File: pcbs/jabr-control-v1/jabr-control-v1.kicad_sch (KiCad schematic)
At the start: 0 parts

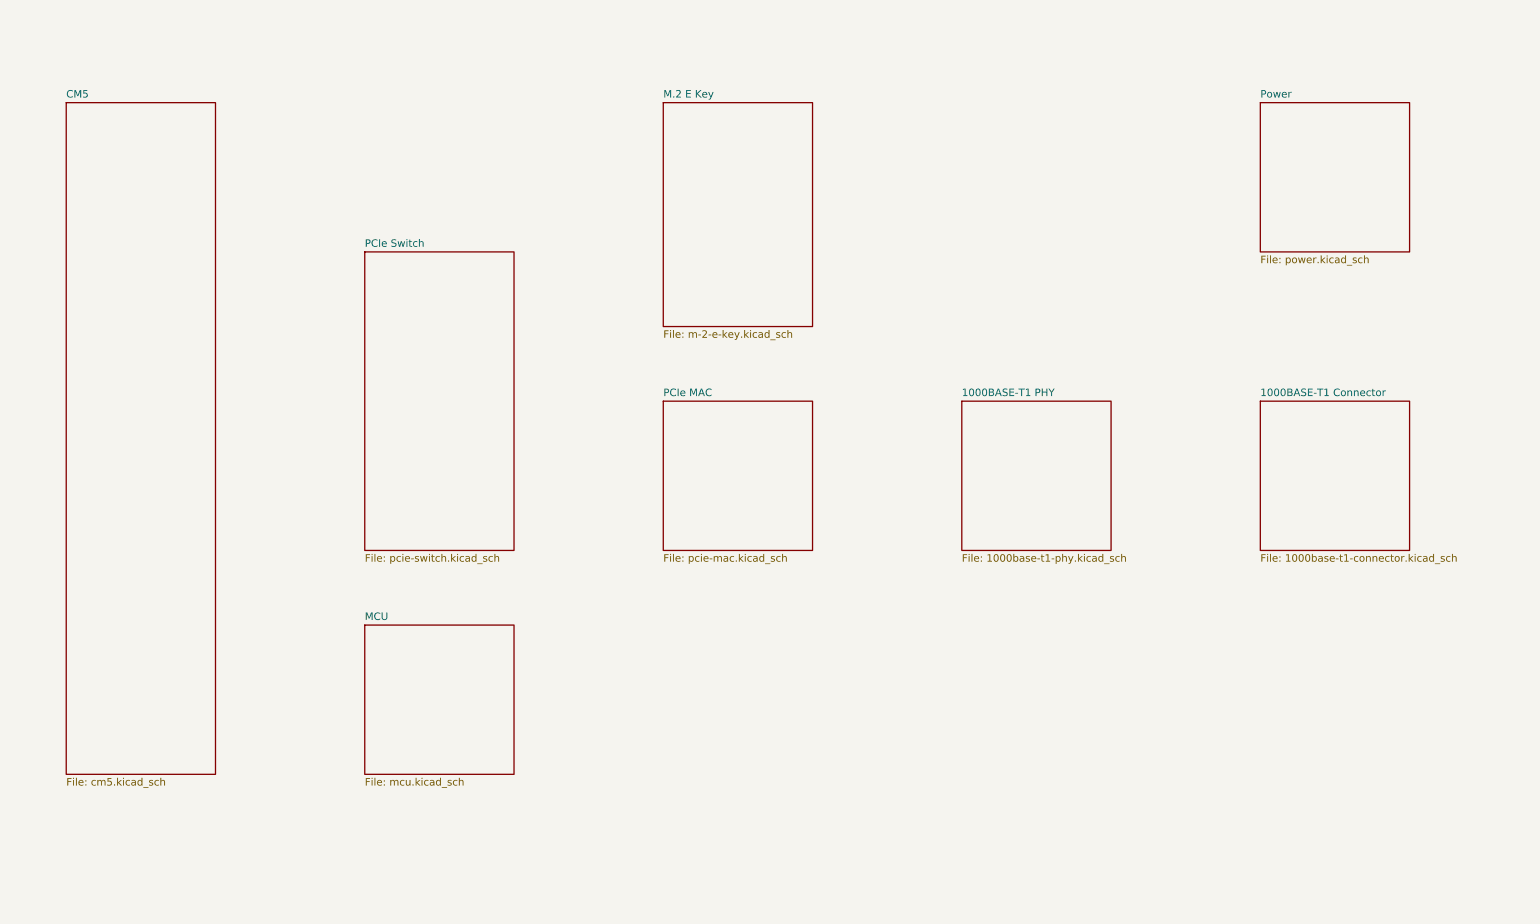
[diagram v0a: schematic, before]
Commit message: Added PCIe connections
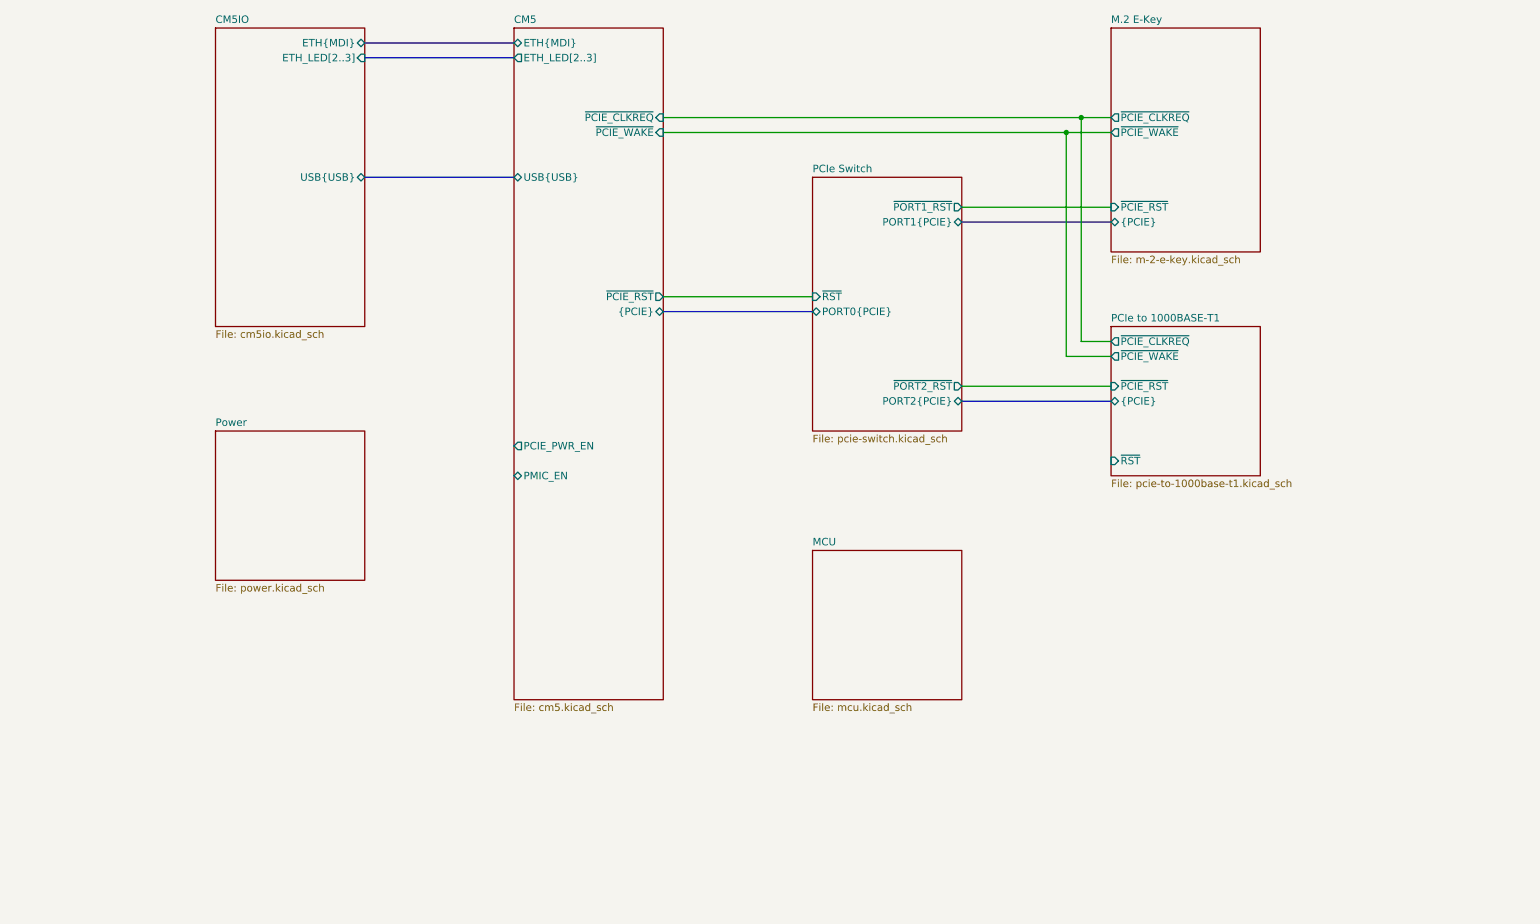
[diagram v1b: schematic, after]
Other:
- sheet M.2 E Key renamed M.2 E-Key
- removed sheet 1000BASE-T1 Connector
- removed sheet 1000BASE-T1 PHY
- removed sheet PCIe MAC
- added sheet CM5IO (cm5io.kicad_sch)
- added sheet PCIe to 1000BASE-T1 (pcie-to-1000base-t1.kicad_sch)
- sheet CM5 ports: added ETH_LED[2..3], ETH{MDI}, PCIE_PWR_EN, PMIC_EN, USB{USB}, {PCIE}, ~{PCIE_CLKREQ}, ~{PCIE_RST}, ~{PCIE_WAKE}; removed none
- sheet M.2 E-Key ports: added {PCIE}, ~{PCIE_CLKREQ}, ~{PCIE_RST}, ~{PCIE_WAKE}; removed none
- sheet PCIe Switch ports: added PORT0{PCIE}, PORT1{PCIE}, PORT2{PCIE}, ~{PORT1_RST}, ~{PORT2_RST}, ~{RST}; removed none

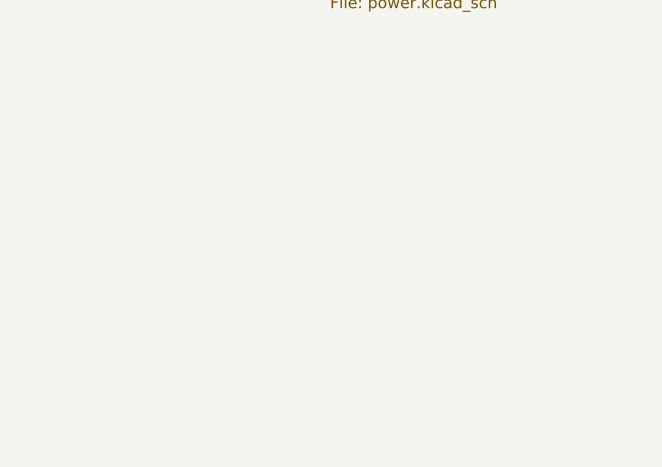
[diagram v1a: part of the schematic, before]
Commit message: Added power sheets
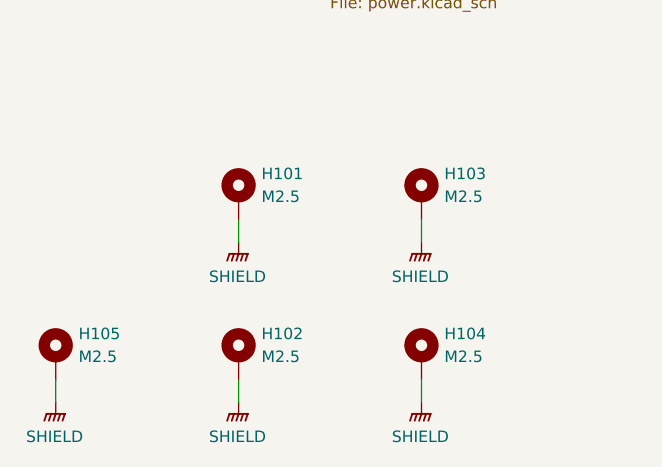
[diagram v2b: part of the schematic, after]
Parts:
- added H101, H102, H103, H104, H105: M2.5, MountingHole:MountingHole_2.7mm_M2.5_Pad, symbol Mechanical:MountingHole_Pad
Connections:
- new net SHIELD: H101.1, H102.1, H103.1, H104.1, H105.1

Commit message: Worked on power and other areas of the schematic
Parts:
- removed H104: M2.5, MountingHole:MountingHole_2.7mm_M2.5_Pad, symbol Mechanical:MountingHole_Pad
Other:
- removed sheet MCU
- sheet CM5 ports: added VBUS_EN, ~{RST}; removed PMIC_EN
- sheet PCIe to 1000BASE-T1 ports: added INH; removed none
- sheet Power ports: added 3V3_M2_EN, INH; removed none
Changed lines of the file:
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@@
 	(wire
 		(pts
-			(xy 73.66 175.26) (xy 73.66 177.8)
+			(xy 139.7 116.84) (xy 215.9 116.84)
 		)
 		(stroke
@@
 	(wire
 		(pts
+			(xy 88.9 109.22) (xy 114.3 109.22)
+		)
+		(stroke
+			(width 0)
+			(type default)
+		)
+	)
+	(wire
+		(pts
 			(xy 210.82 91.44) (xy 210.82 53.34)
 		)
@@
 		(pts
 			(xy 190.5 99.06) (xy 215.9 99.06)
+		)
+		(stroke
+			(width 0)
+			(type default)
+		)
+	)
+	(wire
+		(pts
+			(xy 88.9 129.54) (xy 215.9 129.54)
 		)
 		(stroke
@@
 	)
 	(symbol
-		(lib_id "PWR-SYM:SHIELD")
-		(at 73.66 177.8 0)
-		(unit 1)
-		(exclude_from_sim no)
-		(in_bom yes)
-		(on_board yes)
-		(dnp no)
-		(fields_autoplaced yes)
-		(property "Reference" "#PWR0108"
-			(at 73.66 182.88 0)
-			(effects
-				(font
-					(size 1.27 1.27)
-				)
-				(hide yes)
-			)
-		)
-		(property "Value" "SHIELD"
-			(at 73.533 181.61 0)
-			(effects
-				(font
-					(size 1.27 1.27)
-				)
-			)
-		)
-		(property "Footprint" ""
-			(at 73.66 179.07 0)
-			(effects
-				(font
-					(size 1.27 1.27)
-				)
-				(hide yes)
-			)
-		)
-		(property "Datasheet" ""
-			(at 73.66 179.07 0)
-			(effects
-				(font
-					(size 1.27 1.27)
-				)
-				(hide yes)
-			)
-		)
-		(property "Description" "Power symbol creates a global label with name \"SHIELD\" , global ground"
-			(at 73.66 177.8 0)
-			(effects
-				(font
-					(size 1.27 1.27)
-				)
-				(hide yes)
-			)
-		)
-		(pin "1"
-		)
-		(instances
-			(project "jabr-control-v1"
-				(path "/f91ec272-d09a-4038-bbbb-962739a92c51"
-					(reference "#PWR0108")
-					(unit 1)
-				)
-			)
-		)
-	)
-	(symbol
 		(lib_id "Mechanical:MountingHole_Pad")
 		(at 53.34 172.72 0)
@@
 	(symbol
 		(lib_id "Mechanical:MountingHole_Pad")
-		(at 73.66 172.72 0)
-		(unit 1)
-		(exclude_from_sim no)
-		(in_bom no)
-		(on_board yes)
-		(dnp no)
-		(fields_autoplaced yes)
-		(property "Reference" "H104"
-			(at 76.2 170.1799 0)
-			(effects
-				(font
-					(size 1.27 1.27)
-				)
-				(justify left)
-			)
-		)
-		(property "Value" "M2.5"
-			(at 76.2 172.7199 0)
-			(effects
-				(font
-					(size 1.27 1.27)
-				)
-				(justify left)
-			)
-		)
-		(property "Footprint" "MountingHole:MountingHole_2.7mm_M2.5_Pad"
-			(at 73.66 172.72 0)
-			(effects
-				(font
-					(size 1.27 1.27)
-				)
-				(hide yes)
-			)
-		)
-		(property "Datasheet" "~"
-			(at 73.66 172.72 0)
-			(effects
-				(font
-					(size 1.27 1.27)
-				)
-				(hide yes)
-			)
-		)
-		(property "Description" "Mounting Hole with connection"
-			(at 73.66 172.72 0)
-			(effects
-				(font
-					(size 1.27 1.27)
-				)
-				(hide yes)
-			)
-		)
-		(pin "1"
-		)
-		(instances
-			(project "jabr-control-v1"
-				(path "/f91ec272-d09a-4038-bbbb-962739a92c51"
-					(reference "H104")
-					(unit 1)
-				)
-			)
-		)
-	)
-	(symbol
-		(lib_id "Mechanical:MountingHole_Pad")
 		(at 33.02 172.72 0)
 		(unit 1)
@@
 	)
 	(sheet
-		(at 165.1 127)
-		(size 25.4 25.4)
-		(exclude_from_sim no)
-		(in_bom yes)
-		(on_board yes)
-		(dnp no)
-		(fields_autoplaced yes)
-		(stroke
-			(width 0.1524)
-			(type solid)
-		)
-		(fill
-			(color 0 0 0 0.0000)
-		)
-		(property "Sheetname" "MCU"
-			(at 165.1 126.2884 0)
-			(effects
-				(font
-					(size 1.27 1.27)
-				)
-				(justify left bottom)
-			)
-		)
-		(property "Sheetfile" "mcu.kicad_sch"
-			(at 165.1 152.9846 0)
-			(effects
-				(font
-					(size 1.27 1.27)
-				)
-				(justify left top)
-			)
-		)
-		(instances
-			(project "jabr-control-v1"
-				(path "/f91ec272-d09a-4038-bbbb-962739a92c51"
-					(page "7")
-				)
-			)
-		)
-	)
-	(sheet
 		(at 215.9 38.1)
 		(size 25.4 38.1)
@@
 	(sheet
 		(at 215.9 88.9)
-		(size 25.4 25.4)
+		(size 25.4 43.18)
 		(exclude_from_sim no)
 		(in_bom yes)
@@
 		)
 		(property "Sheetfile" "pcie-to-1000base-t1.kicad_sch"
-			(at 215.9 114.8846 0)
+			(at 215.9 132.6646 0)
 			(effects
 				(font
@@
 		)
 		(pin "~{RST}" input
-			(at 215.9 111.76 180)
+			(at 215.9 116.84 180)
+			(effects
+				(font
+					(size 1.27 1.27)
+				)
+				(justify left)
+			)
+		)
+		(pin "INH" output
+			(at 215.9 129.54 180)
 			(effects
 				(font
@@
 			)
 		)
+		(pin "3V3_M2_EN" input
+			(at 88.9 109.22 0)
+			(effects
+				(font
+					(size 1.27 1.27)
+				)
+				(justify right)
+			)
+		)
+		(pin "INH" input
+			(at 88.9 129.54 0)
+			(effects
+				(font
+					(size 1.27 1.27)
+				)
+				(justify right)
+			)
+		)
 		(instances
 			(project "jabr-control-v1"
@@
 	(sheet
 		(at 114.3 38.1)
-		(size 25.4 114.3)
+		(size 25.4 81.28)
 		(exclude_from_sim no)
 		(in_bom yes)
@@
 		)
 		(property "Sheetfile" "cm5.kicad_sch"
-			(at 114.3 152.9846 0)
+			(at 114.3 119.9646 0)
 			(effects
 				(font
@@
 			)
 		)
-		(pin "PMIC_EN" bidirectional
-			(at 114.3 114.3 180)
-			(effects
-				(font
-					(size 1.27 1.27)
-				)
-				(justify left)
-			)
-		)
+		(pin "VBUS_EN" output
+			(at 114.3 66.04 180)
+			(effects
+				(font
+					(size 1.27 1.27)
+				)
+				(justify left)
+			)
+		)
+		(pin "~{RST}" output
+			(at 139.7 116.84 0)
+			(effects
+				(font
+					(size 1.27 1.27)
+				)
+				(justify right)
+			)
+		)

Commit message: Various small updates
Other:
- sheet CM5 ports: added I2C2{I2C}; removed none
- sheet PCIe Switch ports: added SMB{I2C}; removed none
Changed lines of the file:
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@@
+		)
+	)
+	(bus
+		(pts
+			(xy 139.7 91.44) (xy 165.1 91.44)
+		)
+		(stroke
+			(width 0)
+			(type default)
 		)
 	)
@@
 			)
 		)
+		(pin "SMB{I2C}" bidirectional
+			(at 165.1 91.44 180)
+			(effects
+				(font
+					(size 1.27 1.27)
+				)
+				(justify left)
+			)
+		)
 		(instances
 			(project "jabr-control-v1"
@@
 			(effects
 				(font
+					(size 1.27 1.27)
+				)
+				(justify right)
+			)
+		)
+		(pin "I2C2{I2C}" bidirectional
+			(at 139.7 91.44 0)
+			(effects
+				(font

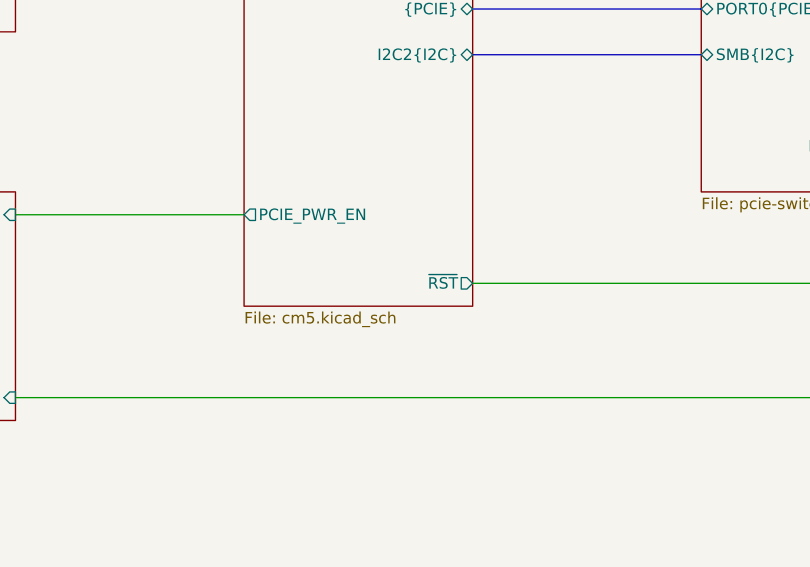
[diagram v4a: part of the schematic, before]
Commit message: Progress on LAN7431 power
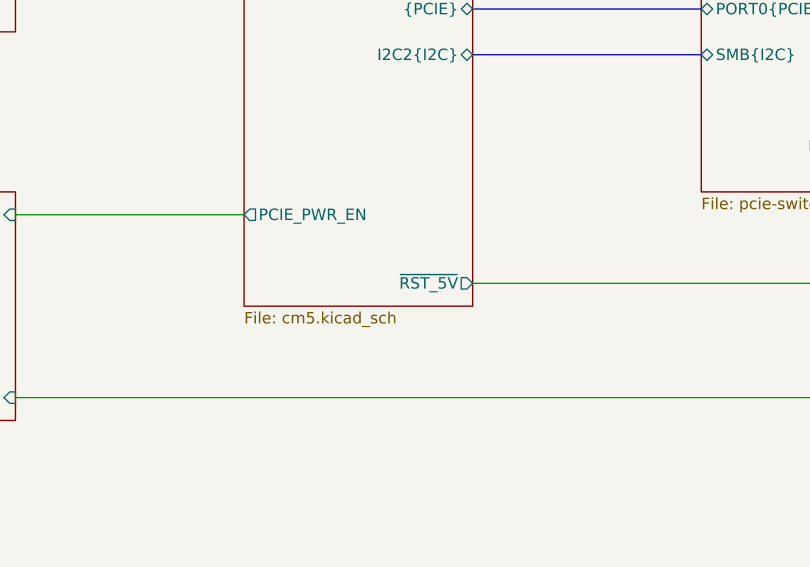
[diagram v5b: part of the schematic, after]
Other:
- sheet CM5 ports: added ~{RST_5V}; removed ~{RST}
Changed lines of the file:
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@@
 			)
 		)
-		(pin "~{RST}" output
-			(at 139.7 116.84 0)
+		(pin "I2C2{I2C}" bidirectional
+			(at 139.7 91.44 0)
 			(effects
 				(font
@@
 			)
 		)
-		(pin "I2C2{I2C}" bidirectional
-			(at 139.7 91.44 0)
+		(pin "~{RST_5V}" output
+			(at 139.7 116.84 0)
 			(effects
 				(font

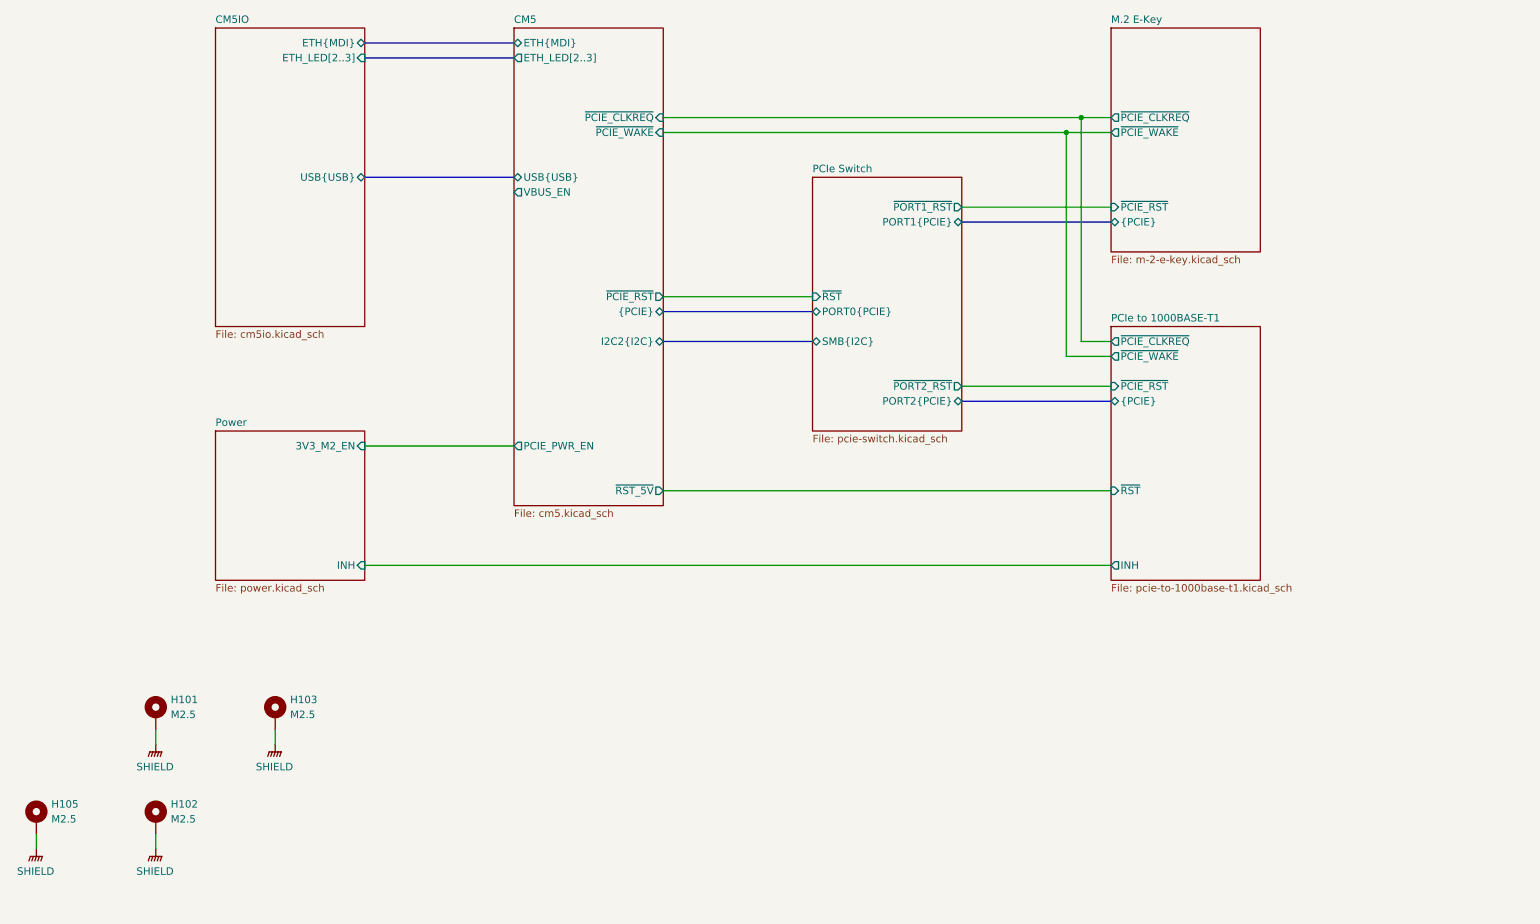
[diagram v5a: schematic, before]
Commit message: Finished M.2 E-Key schematic
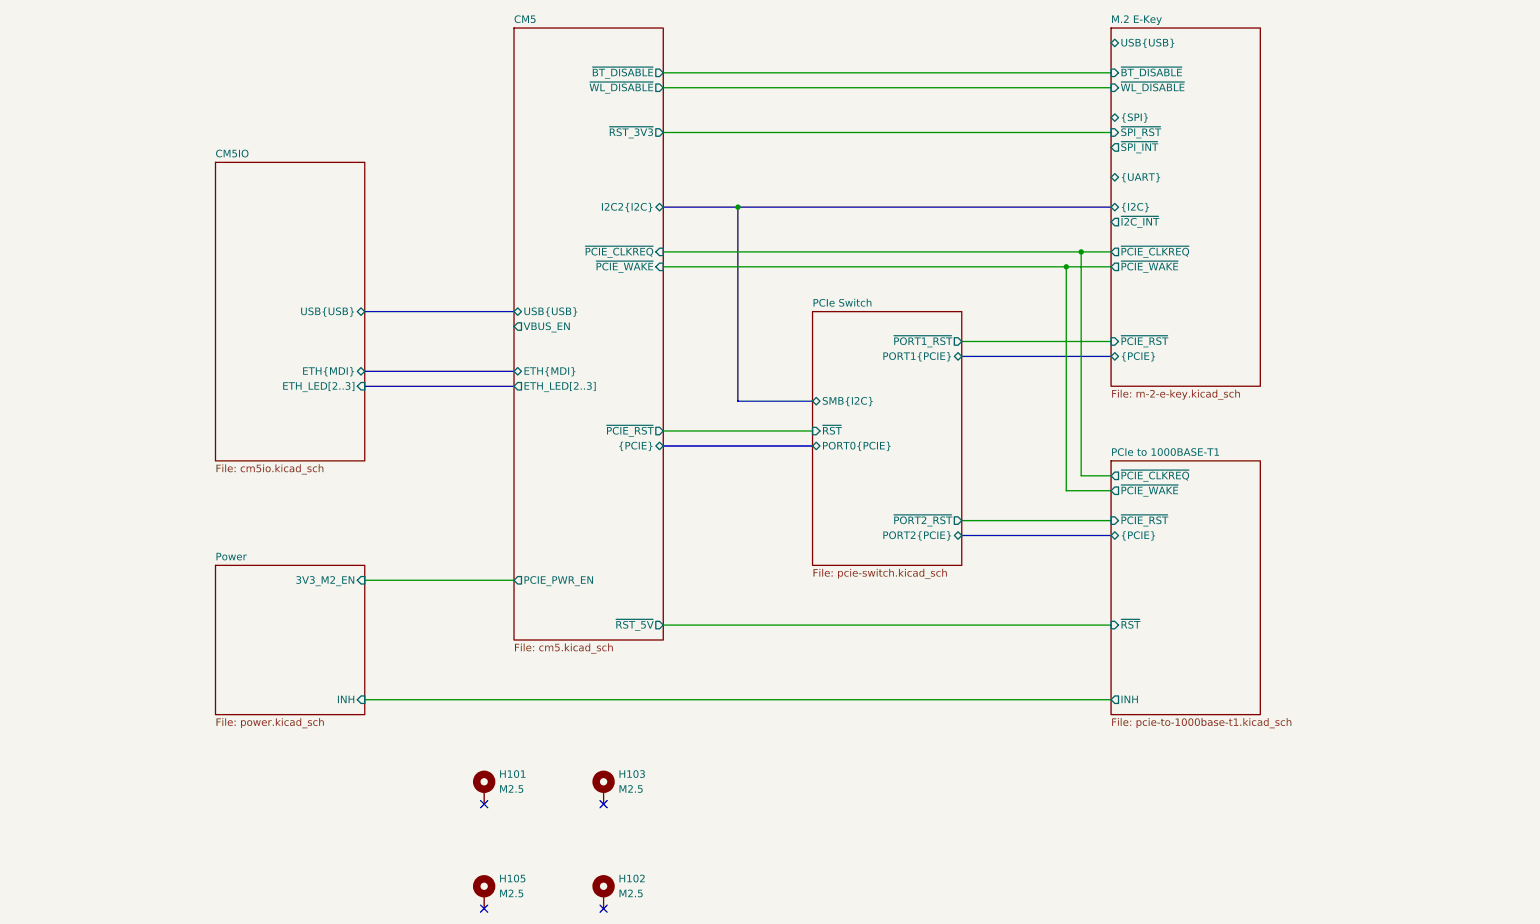
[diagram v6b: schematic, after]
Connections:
- removed net SHIELD: H101.1, H102.1, H103.1, H105.1
- no-connect marks 0 -> 4
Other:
- sheet CM5 ports: added ~{BT_DISABLE}, ~{RST_3V3}, ~{WL_DISABLE}; removed none
- sheet M.2 E-Key ports: added USB{USB}, {I2C}, {SPI}, {UART}, ~{BT_DISABLE}, ~{I2C_INT}, ~{SPI_INT}, ~{SPI_RST}, ~{WL_DISABLE}; removed none
- moved on the sheet: H101, H102, H103, H105
